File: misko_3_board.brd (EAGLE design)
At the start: 74 x 152 mm, 179 parts, among them IC1 ATMEGA1281-16AU, IC10 ORG1510-MK4, IC11 TPS3808G33DBVT, IC12 LTC4425, IC13 RN-42, IC14 ADXL345, IC15 74HCT1G32, IC16 FM25W256-SOIC, IC17 MICROSD_SPI_MODE, IC18 FH12-30S-0.5SH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

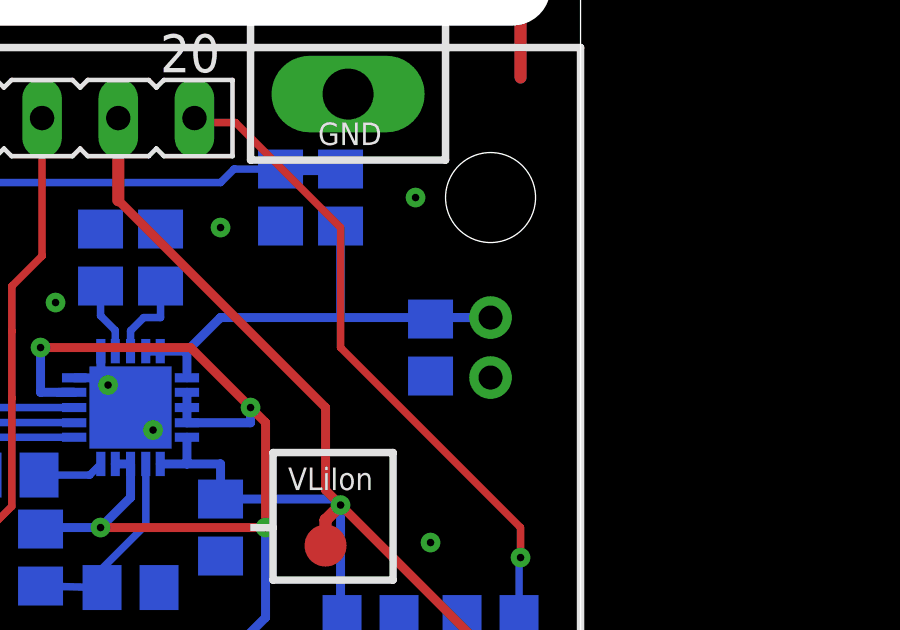
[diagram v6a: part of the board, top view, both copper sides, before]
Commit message: - corrected position of liion bypass cap
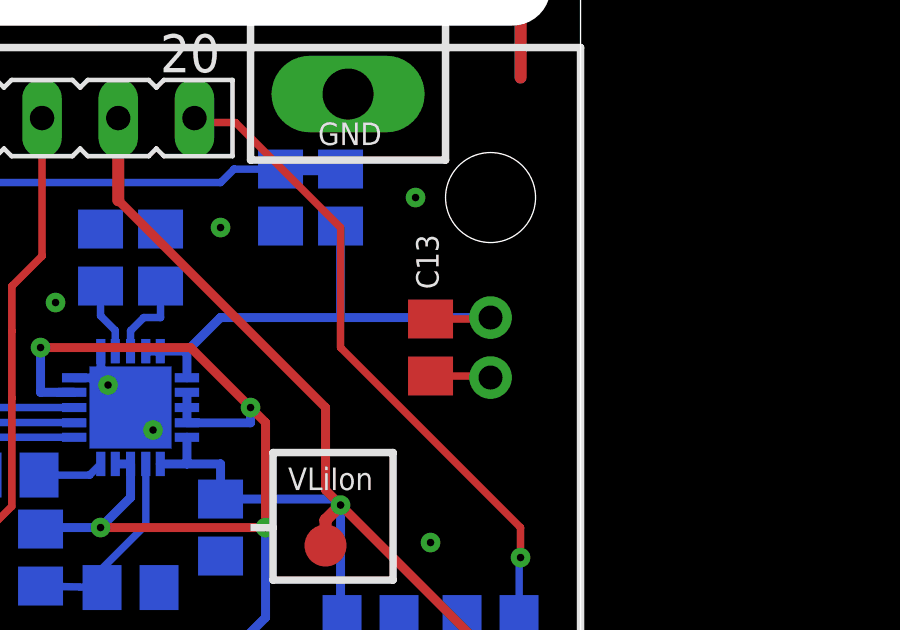
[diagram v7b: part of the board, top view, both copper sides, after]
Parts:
- flipped C13 to the top
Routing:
- net GND: track 131.3 -> 133.3 mm
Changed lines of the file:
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@@
 <layer number="19" name="Unrouted" color="6" fill="1" visible="yes" active="yes"/>
 <layer number="20" name="Dimension" color="15" fill="1" visible="yes" active="yes"/>
-<layer number="21" name="tPlace" color="7" fill="1" visible="no" active="yes"/>
+<layer number="21" name="tPlace" color="7" fill="1" visible="yes" active="yes"/>
 <layer number="22" name="bPlace" color="7" fill="1" visible="yes" active="yes"/>
-<layer number="23" name="tOrigins" color="15" fill="1" visible="no" active="yes"/>
+<layer number="23" name="tOrigins" color="15" fill="1" visible="yes" active="yes"/>
 <layer number="24" name="bOrigins" color="15" fill="1" visible="yes" active="yes"/>
-<layer number="25" name="tNames" color="7" fill="1" visible="no" active="yes"/>
+<layer number="25" name="tNames" color="7" fill="1" visible="yes" active="yes"/>
 <layer number="26" name="bNames" color="7" fill="1" visible="yes" active="yes"/>
 <layer number="27" name="tValues" color="7" fill="1" visible="no" active="yes"/>
@@
 <attribute name="VALUE" x="64.54" y="25.27" size="1.27" layer="28" rot="MR270"/>
 </element>
-<element name="C13" library="resistor" package="C0805" value="10µF" x="69" y="30" smashed="yes" rot="MR270">
-<attribute name="NAME" x="69.48" y="33.77" size="0.75" layer="26" rot="MR270"/>
-<attribute name="VALUE" x="71.54" y="31.27" size="1.27" layer="28" rot="MR270"/>
+<element name="C13" library="resistor" package="C0805" value="10µF" x="69" y="30" smashed="yes" rot="R270">
+<attribute name="NAME" x="68.52" y="33.77" size="0.75" layer="25" rot="R270"/>
+<attribute name="VALUE" x="66.46" y="31.27" size="1.27" layer="27" rot="R270"/>
 </element>
 <element name="C14" library="resistor" package="C0805" value="0.1µF" x="40" y="32" smashed="yes" rot="R90">
@@
 <wire x1="60.8796" y1="29.8796" x2="62" y2="31" width="0.3" layer="16"/>
 <wire x1="62" y1="31" x2="66" y2="31" width="0.3" layer="16"/>
-<wire x1="71" y1="31" x2="69.05" y2="31" width="0.3" layer="16"/>
-<wire x1="69.05" y1="31" x2="69" y2="30.95" width="0.3" layer="16"/>
+<wire x1="69" y1="30.95" x2="71" y2="30.95" width="0.25" layer="1"/>
+<wire x1="71" y1="30.95" x2="71" y2="31" width="0.25" layer="1"/>
 </signal>
 <signal name="VGPS" class="1">
@@
 <contactref element="C47" pad="-"/>
 <contactref element="CONN10" pad="2"/>
+<wire x1="69" y1="29.05" x2="71" y2="29.05" width="0.25" layer="1"/>
+<wire x1="71" y1="29.05" x2="71" y2="29" width="0.25" layer="1"/>
 <wire x1="135" y1="45.43" x2="147" y2="45.43" width="0" layer="19" extent="1-1"/>
 <wire x1="123" y1="45.43" x2="135" y2="45.43" width="0" layer="19" extent="1-1"/>

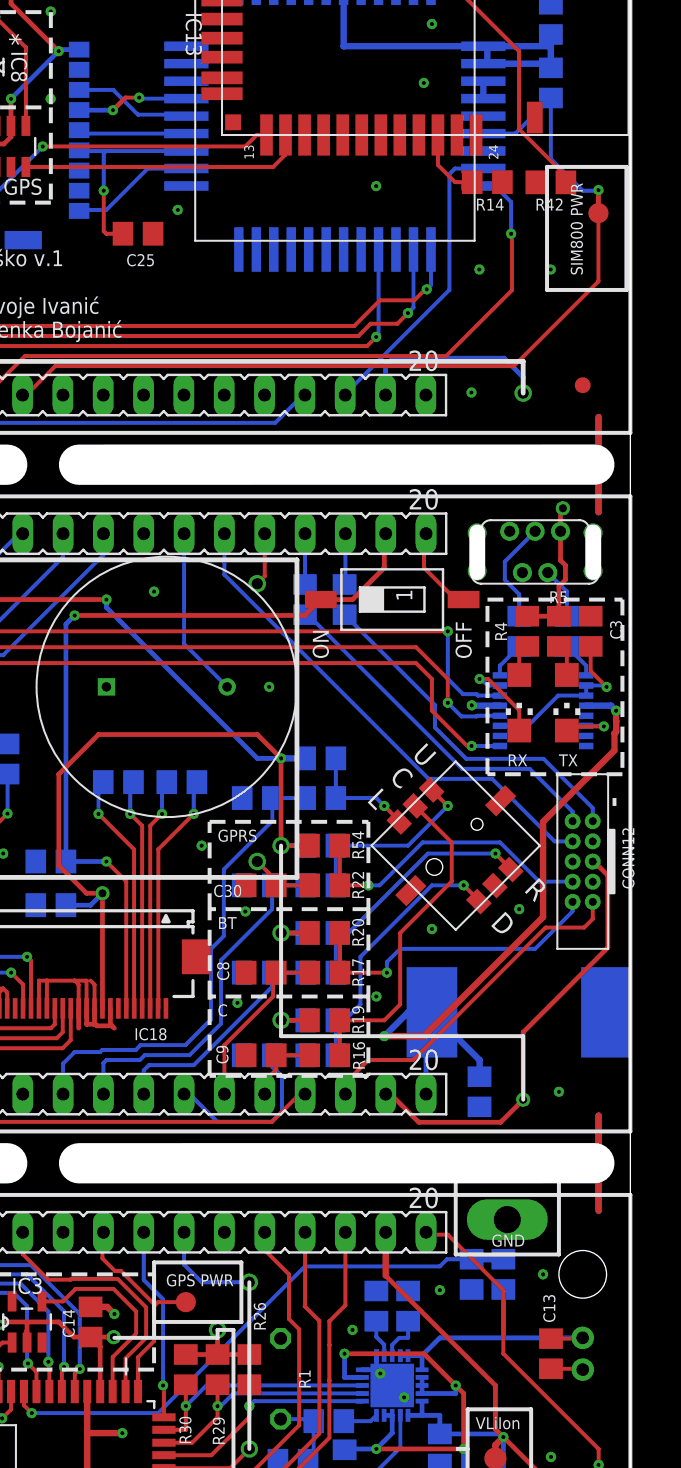
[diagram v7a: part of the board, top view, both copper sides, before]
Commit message: - corrected a few widths, buzzer holes
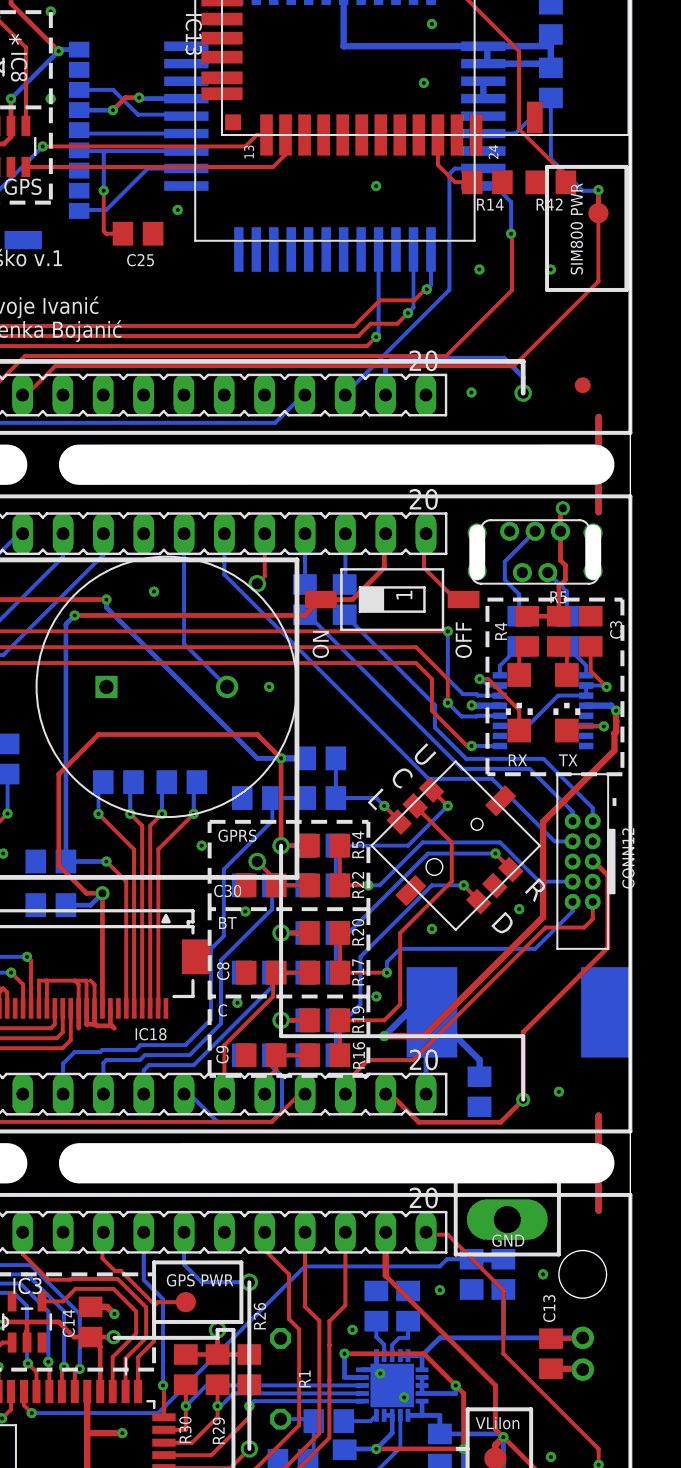
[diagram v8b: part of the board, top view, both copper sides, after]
